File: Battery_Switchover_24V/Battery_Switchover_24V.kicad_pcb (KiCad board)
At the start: 2 copper layers, 73 parts, among them J1 USB_C_Receptacle_USB2.0_14P, U1 OPA2197xD, U10 ACS37002LMABTR-066B5, U11 LM60CIM3, U12 L5973D, U13 AMS1117-3.3, U14 OPA2197xD, U3 LPC11U14FBD48-201, U4 LM74610QDGKRQ1, U5 FDBL86066-F085, U6 LM74610QDGKRQ1, U7 FDBL86066-F085, U8 ACS37002LMABTR-066B5, U9 ACS37002LMABTR-066B5, Y1 12.000MHz

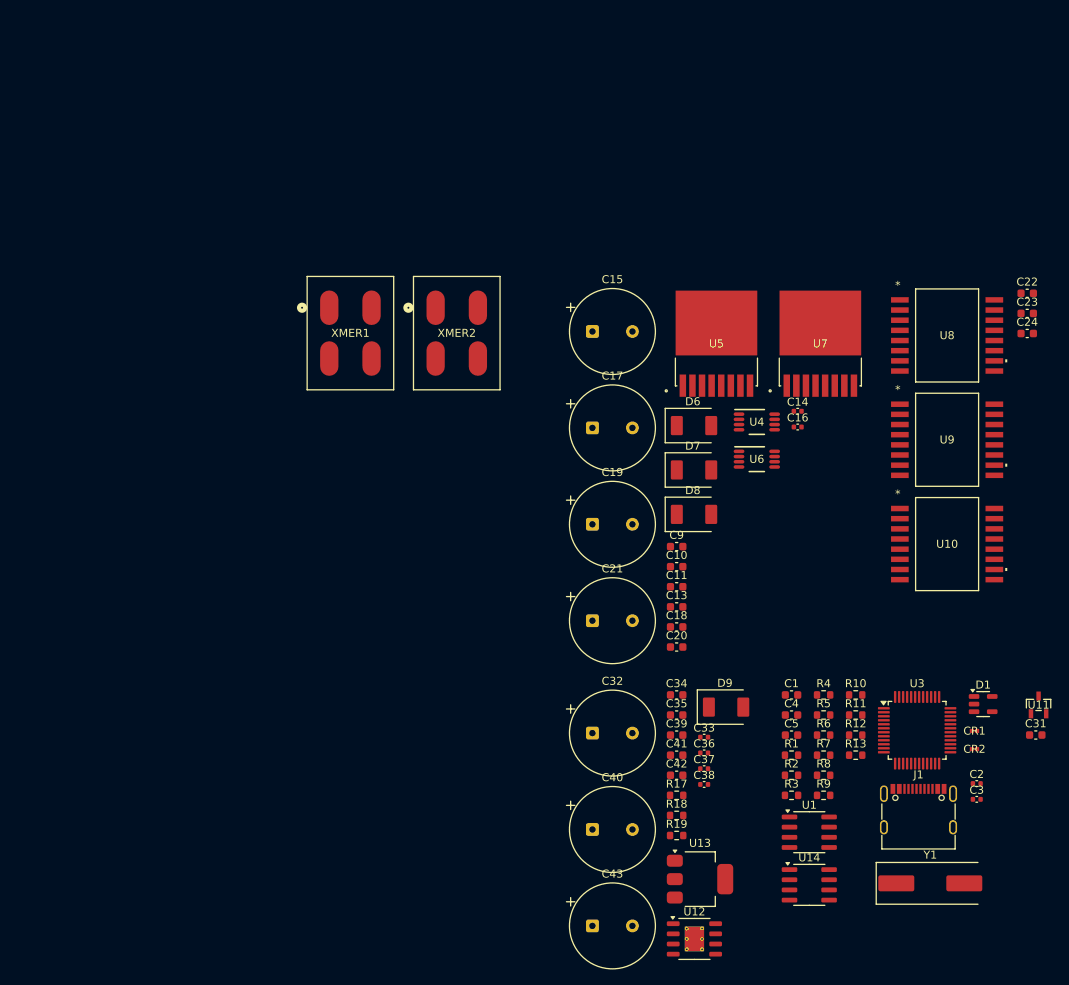
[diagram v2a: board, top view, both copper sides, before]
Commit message: Added Footprints to the remaining parts calculated the current IC's resistance and capcitances
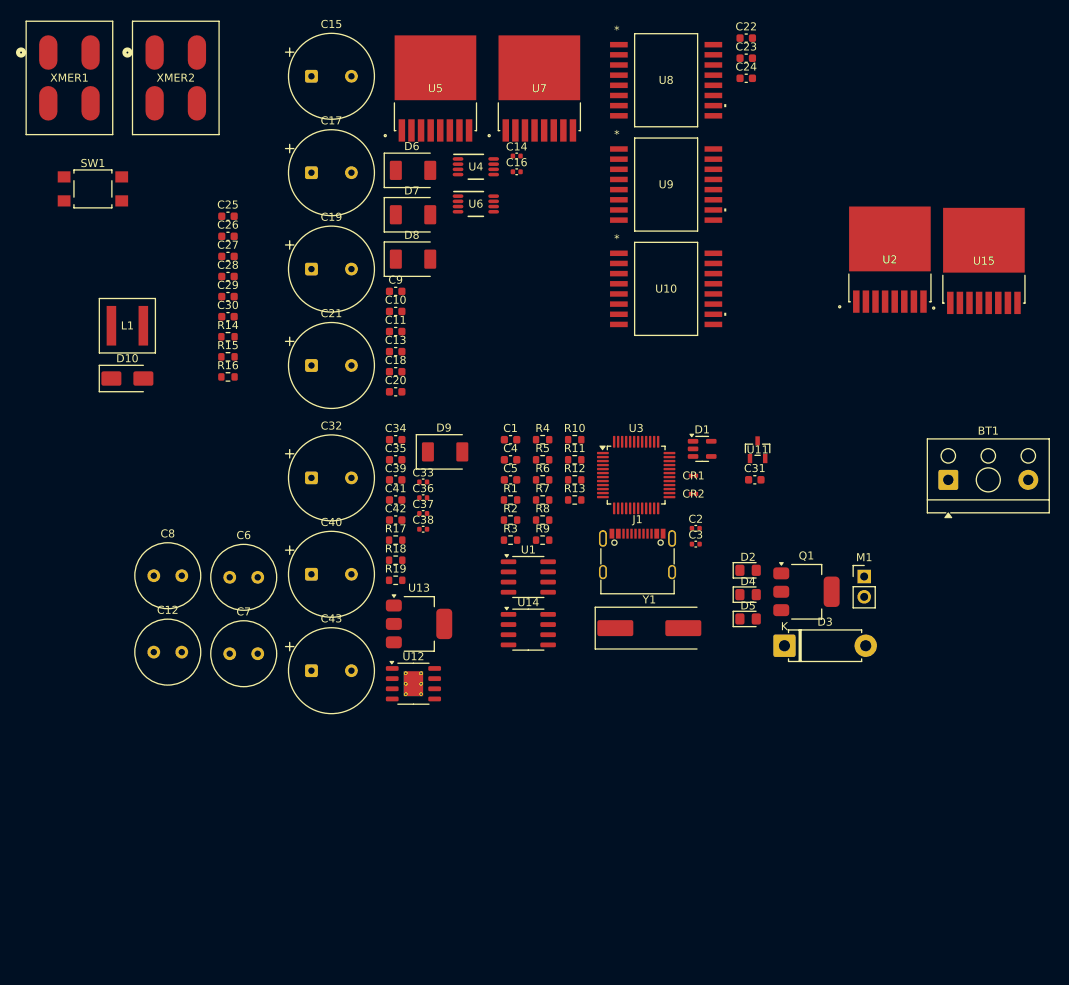
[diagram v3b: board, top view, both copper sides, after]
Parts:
- added BT1: Battery_Cell, TerminalBlock_RND:TerminalBlock_RND_205-00023_1x02_P10.00mm_Horizontal, F.Cu at (128.8, 71.4)
- added C12: 2.2uf, Capacitor_THT:C_Radial_D8.0mm_H7.0mm_P3.50mm, F.Cu at (29.5, 92.9)
- added C25: 6nF, Capacitor_SMD:C_0603_1608Metric, F.Cu at (38.8, 38.4)
- added C26: 6nF, Capacitor_SMD:C_0603_1608Metric, F.Cu at (38.8, 40.9)
- added C27: 6nF, Capacitor_SMD:C_0603_1608Metric, F.Cu at (38.8, 43.4)
- added C28: 6nF, Capacitor_SMD:C_0603_1608Metric, F.Cu at (38.8, 45.9)
- added C29: 6nF, Capacitor_SMD:C_0603_1608Metric, F.Cu at (38.8, 48.5)
- added C30: 6nF, Capacitor_SMD:C_0603_1608Metric, F.Cu at (38.8, 51.0)
- added C6: 10uF, Capacitor_THT:C_Radial_D8.0mm_H7.0mm_P3.50mm, F.Cu at (39.0, 83.5)
- added C7: 10uF, Capacitor_THT:C_Radial_D8.0mm_H7.0mm_P3.50mm, F.Cu at (39.0, 93.1)
- added C8: 2.2uf, Capacitor_THT:C_Radial_D8.0mm_H7.0mm_P3.50mm, F.Cu at (29.5, 83.3)
- added D10: D_Schottky, Diode_SMD:D_SMA, F.Cu at (26.2, 58.7)
- added D2: LED, LED_SMD:LED_0805_2012Metric_Pad1.15x1.40mm_HandSolder, F.Cu at (103.8, 82.7)
- added D3: 1N4007, Diode_THT:D_5W_P10.16mm_Horizontal, F.Cu at (108.3, 92.1)
- added D4: LED, LED_SMD:LED_0805_2012Metric_Pad1.15x1.40mm_HandSolder, F.Cu at (103.8, 85.7)
- added D5: LED, LED_SMD:LED_0805_2012Metric_Pad1.15x1.40mm_HandSolder, F.Cu at (103.8, 88.8)
- added L1: 15uH, footprints:IND_XAL6060_COC-L, F.Cu at (26.2, 52.1)
- added M1: Fan, Connector_PinHeader_2.54mm:PinHeader_1x02_P2.54mm_Vertical, F.Cu at (118.3, 83.4)
- added Q1: PZT2222AT1G, Package_TO_SOT_SMD:SOT-223-3_TabPin2, F.Cu at (111.1, 85.4)
- added R14: 100K, Resistor_SMD:R_0603_1608Metric, F.Cu at (38.8, 53.5)
- added R15: 100K, Resistor_SMD:R_0603_1608Metric, F.Cu at (38.8, 56.0)
- added R16: 100K, Resistor_SMD:R_0603_1608Metric, F.Cu at (38.8, 58.5)
- added SW1: SW_Push, Button_Switch_SMD:SW_SPST_TL3305A, F.Cu at (21.9, 35.0)
- added U15: FDBL86066-F085, footprints:H-PSOF8L_ONS, F.Cu at (133.2, 44.0)
- added U2: FDBL86066-F085, footprints:H-PSOF8L_ONS, F.Cu at (121.5, 43.8)
- moved C31 47.4 mm to (104.6, 71.4)
- moved CR1 47.4 mm to (96.9, 70.8)
- moved CR2 47.4 mm to (96.9, 73.1)
- moved U11 47.4 mm to (105.0, 67.6)
- moved C42 47.4 mm to (59.7, 76.4)
- moved R2 47.4 mm to (74.1, 76.4)
- moved R8 47.4 mm to (78.1, 76.4)
- moved C1 47.4 mm to (74.1, 66.3)
- moved C10 47.4 mm to (59.7, 50.3)
- moved C11 47.4 mm to (59.7, 52.8)
- moved C14 47.4 mm to (74.9, 30.9)
- moved C15 47.4 mm to (49.2, 20.9)
- moved C16 47.4 mm to (74.9, 32.9)
- moved C17 47.4 mm to (49.2, 33.0)
- moved C18 47.4 mm to (59.7, 57.8)
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
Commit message: Added board edge to PCB and some general placement as well as some schematic changes
Added connectors for Vin and for low side current monitoring(3 connectors) (connector types must be changed. Changes to the power controll circuit added bypass capacitor to the opamp. Added output connector
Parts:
- added BT2: Battery_Cell, TerminalBlock_RND:TerminalBlock_RND_205-00023_1x02_P10.00mm_Horizontal, F.Cu at (270.6, 132.5)
- added BT3: Battery_Cell, TerminalBlock_RND:TerminalBlock_RND_205-00023_1x02_P10.00mm_Horizontal, F.Cu at (26.8, 132.8)
- added BT4: Battery_Cell, TerminalBlock_RND:TerminalBlock_RND_205-00023_1x02_P10.00mm_Horizontal, F.Cu at (35.2, 46.5)
- added BT5: Battery_Cell, TerminalBlock_RND:TerminalBlock_RND_205-00023_1x02_P10.00mm_Horizontal, F.Cu at (67.0, 46.5)
- added BT6: Battery_Cell, TerminalBlock_RND:TerminalBlock_RND_205-00023_1x02_P10.00mm_Horizontal, F.Cu at (98.9, 46.5)
- added C44: 100nF, Capacitor_SMD:C_0603_1608Metric, F.Cu at (174.9, 71.3)
- added C45: 100nF, Capacitor_SMD:C_0603_1608Metric, F.Cu at (174.9, 73.8)
- D2, D4, D5, R11, R12, R13: moved to B.Cu
- moved XMER1 265.0 mm to (255.3, 132.5), turned to 180 degrees
- moved SW1 249.0 mm to (270.5, 49.0)
- moved D6 210.2 mm to (242.2, 136.9), turned to 90 degrees
- moved C8 201.6 mm to (220.1, 149.0), turned to -90 degrees
- moved C9 198.9 mm to (238.5, 135.0), turned to -90 degrees
- moved U4 196.8 mm to (226.8, 150.8), turned to 90 degrees
- moved R11 191.4 mm to (273.4, 61.9), turned to 180 degrees
- moved R12 191.4 mm to (273.4, 64.4), turned to 180 degrees
- moved R13 191.4 mm to (273.4, 66.9), turned to 180 degrees
- moved U5 190.0 mm to (224.6, 125.0), turned to 90 degrees
- moved XMER2 177.1 mm to (156.9, 141.2), turned to 180 degrees
- moved D2 166.6 mm to (269.0, 61.4), turned to 180 degrees
- moved D4 166.6 mm to (269.0, 64.5), turned to 180 degrees
- moved D5 166.6 mm to (269.0, 67.5), turned to 180 degrees
- moved C11 162.8 mm to (208.0, 120.0), turned to 90 degrees
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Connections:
- U10 pad 1: /Current Monitor/Load_Lovv -> Load3
- U10 pad 2: /Current Monitor/Load_Lovv -> Load3
- U10 pad 3: /Current Monitor/Load_Lovv -> Load3
- U10 pad 4: /Current Monitor/Load_Lovv -> Load3
- U15 pad 9: Net-(D6-A2) -> Vbatt
- U2 pad 9: Vbatt -> Net-(D6-A2)
- U6 pad 8: Vbatt -> Net-(D6-A2)
- U7 pad 9: Vbatt -> Net-(D6-A2)
- U8 pad 1: /Current Monitor/Load_Lovv -> Load1
- U8 pad 2: /Current Monitor/Load_Lovv -> Load1
- U8 pad 3: /Current Monitor/Load_Lovv -> Load1
- U8 pad 4: /Current Monitor/Load_Lovv -> Load1
- U9 pad 1: /Current Monitor/Load_Lovv -> Load2
- U9 pad 2: /Current Monitor/Load_Lovv -> Load2
- U9 pad 3: /Current Monitor/Load_Lovv -> Load2
- U9 pad 4: /Current Monitor/Load_Lovv -> Load2
- XMER2 pad 1: Vbatt -> Net-(D6-A2)
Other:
- board outline added: 260.5 x 131 mm

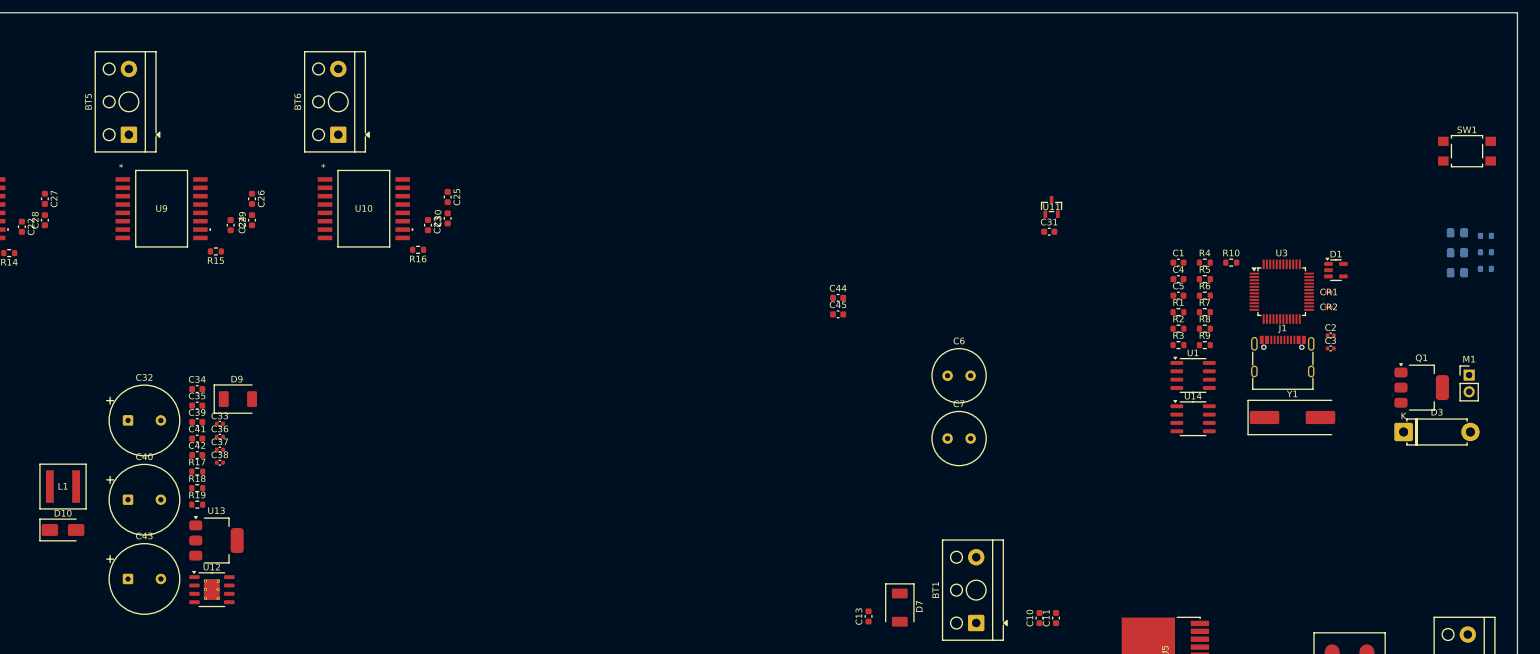
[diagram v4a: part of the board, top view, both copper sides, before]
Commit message: Fixed opamp footprint issue done some preliminary placement
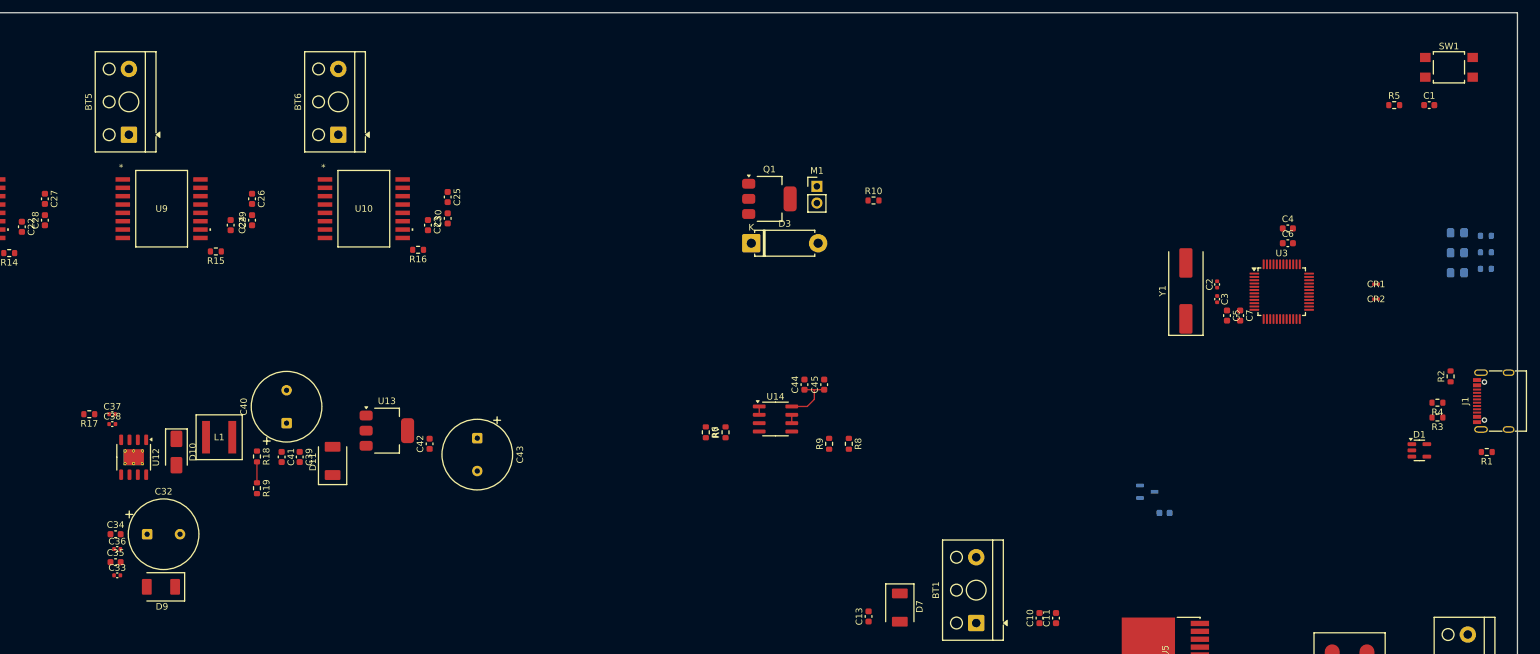
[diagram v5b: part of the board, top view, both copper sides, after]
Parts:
- removed U1: OPA2197xD, Package_SO:SOIC-8_3.9x4.9mm_P1.27mm
- added D11: ~, footprints:P26_DO-214AA_SMB, F.Cu at (98.0, 98.2)
- C31, U11: moved to B.Cu
- C6, C7: footprint Capacitor_THT:C_Radial_D8.0mm_H7.0mm_P3.50mm -> Capacitor_SMD:C_0603_1608Metric
- moved D3 103.3 mm to (161.7, 63.0)
- moved Q1 103.3 mm to (164.4, 56.3)
- moved M1 103.3 mm to (171.6, 54.4)
- moved R6 78.7 mm to (154.8, 91.8), turned to -90 degrees
- moved R7 75.1 mm to (157.8, 91.8), turned to 90 degrees
- moved U14 63.5 mm to (165.3, 89.7)
- moved R9 59.1 mm to (173.5, 93.5), turned to 90 degrees
- moved C43 57.3 mm to (120.0, 92.6), turned to -90 degrees
- moved R8 56.9 mm to (176.5, 93.5), turned to -90 degrees
- moved C6 55.5 mm to (243.2, 63.0)
- moved R10 55.2 mm to (180.2, 56.5)
- moved R1 51.5 mm to (273.5, 94.8), turned to 180 degrees
- moved C7 48.3 mm to (236.0, 74.0), turned to -90 degrees
- moved C31 46.2 mm to (224.5, 104.0)
- moved U11 45.7 mm to (221.9, 100.8), turned to 90 degrees
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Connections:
- CR2 pad 2: Net-(U1B-+) -> Net-(U14B-+)
- R8 pad 1: Net-(U1B-+) -> Net-(U14B-+)
- R9 pad 2: Net-(U1B-+) -> Net-(U14B-+)
- U14 pad 4: (no net) -> GND
- U14 pad 5: (no net) -> Net-(U14B-+)
- U14 pad 6: (no net) -> ADC_In
- U14 pad 7: (no net) -> ADC_In
- U14 pad 8: (no net) -> +5V
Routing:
- net +5V: track 0.00 -> 8.35 mm
- net Net-(U12-FB): track 0.00 -> 3.17 mm
- net ADC_Batt: track 0.00 -> 1.27 mm
- net ADC_In: track 0.00 -> 1.27 mm

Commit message: Some polishes
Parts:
- moved C44 66.8 mm to (235.4, 97.1)
- moved C45 66.8 mm to (238.4, 97.1)
- moved R6 66.8 mm to (220.4, 104.4)
- moved R7 66.8 mm to (223.4, 104.4)
- moved R8 66.8 mm to (242.1, 106.1)
- moved R9 66.8 mm to (239.1, 106.1)
- moved U14 66.8 mm to (231.0, 102.3)
- moved D3 46.8 mm to (198.6, 91.7)
- moved M1 46.8 mm to (208.6, 83.1)
- moved Q1 46.8 mm to (201.3, 85.0)
- moved R10 46.8 mm to (217.2, 85.2)
- moved CR1 46.7 mm to (225.5, 104.0), turned to 90 degrees
- moved CR2 36.2 mm to (244.8, 105.7), turned to 90 degrees
- moved C43 28.6 mm to (148.4, 95.9)
- moved C32 28.6 mm to (98.2, 110.5)
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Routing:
- net +5V: track 8.35 -> 0.00 mm
- net Net-(U12-FB): track 3.17 -> 0.00 mm
- net ADC_Batt: track 1.27 -> 0.00 mm
- net ADC_In: track 1.27 -> 0.00 mm

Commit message: Placement changes to shrink the board size
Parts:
- moved C22 154.6 mm to (205.3, 60.0)
- moved C27 154.6 mm to (208.8, 55.8)
- moved C28 154.6 mm to (208.8, 59.0)
- moved R14 154.6 mm to (203.4, 64.0)
- moved U8 154.6 mm to (195.8, 57.2)
- moved BT4 143.3 mm to (178.4, 52.8), turned to -90 degrees
- moved C24 123.9 mm to (204.9, 79.2)
- moved C26 123.9 mm to (208.2, 75.2)
- moved C29 123.9 mm to (208.2, 78.5)
- moved R15 123.9 mm to (202.7, 83.2)
- moved U9 123.9 mm to (194.4, 76.8)
- moved BT5 114.2 mm to (178.4, 71.8), turned to -90 degrees
- moved C23 99.5 mm to (204.3, 98.5)
- moved C25 99.5 mm to (207.3, 94.2)
- moved C30 99.5 mm to (207.3, 97.5)
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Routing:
- net Vbatt: track 0.00 -> 106.1 mm
- net Net-(D6-A2): track 0.00 -> 83.2 mm
- net Net-(U15-G): track 0.00 -> 28.3 mm, vias 0 -> 2
- net Vin: track 0.00 -> 15.3 mm
- net Net-(U6-VCAPH): track 0.00 -> 9.19 mm
- net Net-(U6-VCAPL): track 0.00 -> 8.11 mm
- net Net-(U2-G): track 0.00 -> 4.72 mm
- added copper zone on F.Cu, net Load1

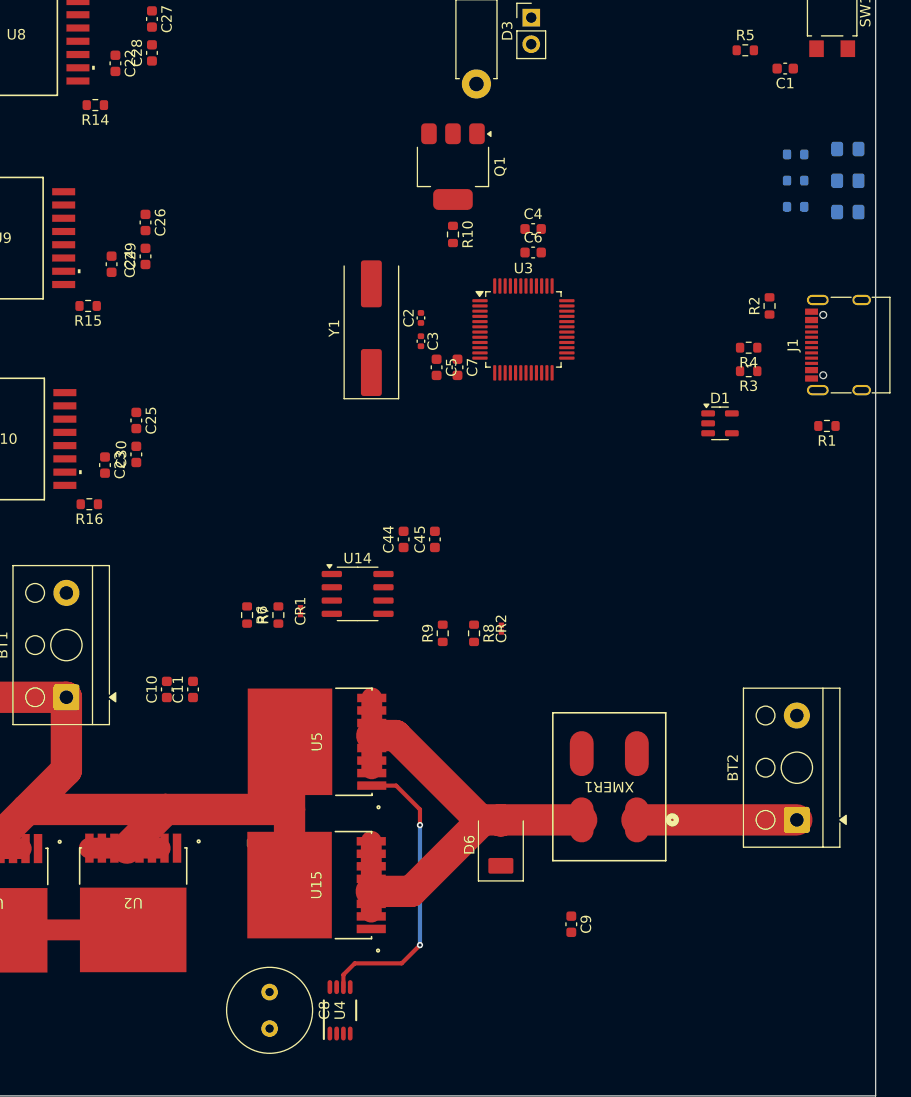
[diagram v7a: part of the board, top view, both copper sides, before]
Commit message: Minor placement changes
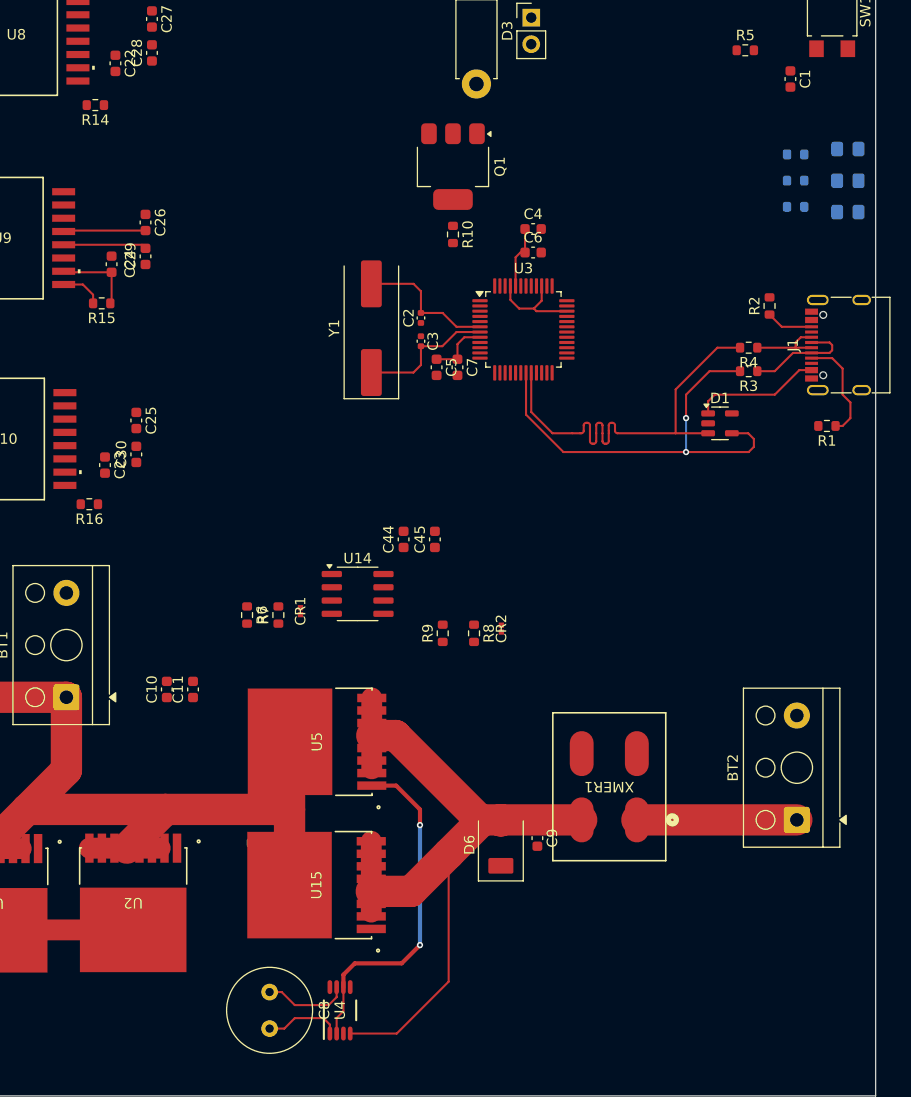
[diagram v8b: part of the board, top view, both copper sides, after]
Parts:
- moved C9 8.87 mm to (245.8, 134.2)
- moved R15 1.33 mm to (204.0, 83.0)
- moved C1 1.12 mm to (270.0, 61.5), turned to -90 degrees
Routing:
- net Net-(U3-USB_DM): track 0.00 -> 42.2 mm, vias 0 -> 2
- net Net-(U3-USB_DP): track 0.00 -> 42.2 mm
- net Net-(D6-A2): track 83.2 -> 107.0 mm
- net +5V: track 0.00 -> 20.0 mm
- net Net-(U3-XTALIN): track 0.00 -> 13.3 mm
- net Net-(U3-XTALOUT): track 0.00 -> 13.1 mm
- net +3.3V: track 0.00 -> 12.0 mm
- net Net-(J1-D--PadA7): track 0.00 -> 10.6 mm
- net Net-(J1-CC1): track 0.00 -> 10.2 mm
- net VREF3: track 0.00 -> 9.66 mm
- net Net-(U4-VCAPH): track 0.00 -> 8.22 mm
- net VIOUT2: track 0.00 -> 7.99 mm
- net VREF2: track 0.00 -> 7.88 mm
- net Net-(J1-D+-PadA6): track 0.00 -> 7.43 mm
- net Net-(U4-VCAPL): track 0.00 -> 7.30 mm
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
